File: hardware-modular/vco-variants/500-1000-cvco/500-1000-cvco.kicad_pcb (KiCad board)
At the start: 2 copper layers, 60 x 40 mm, 5 parts, among them J1 RF_IN

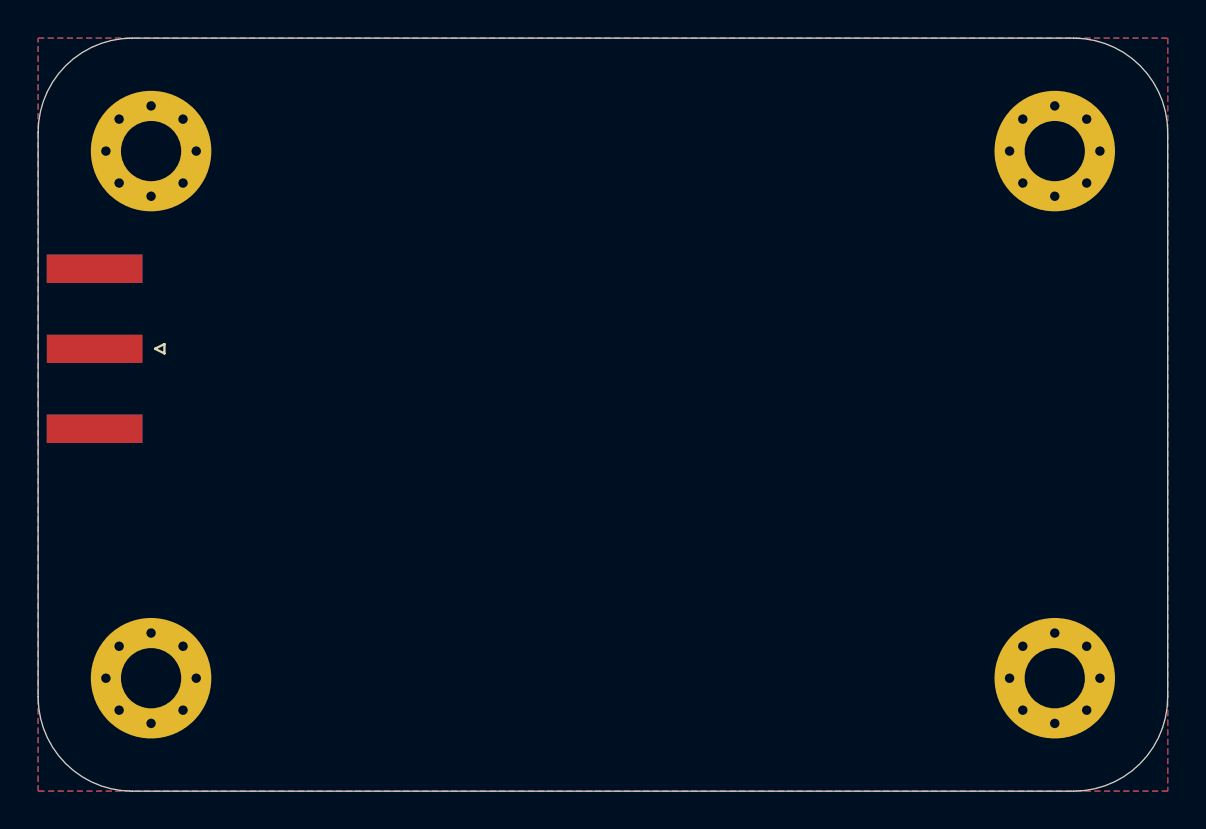
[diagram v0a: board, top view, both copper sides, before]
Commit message: CVCO 500-1000 MHz module - PCB.
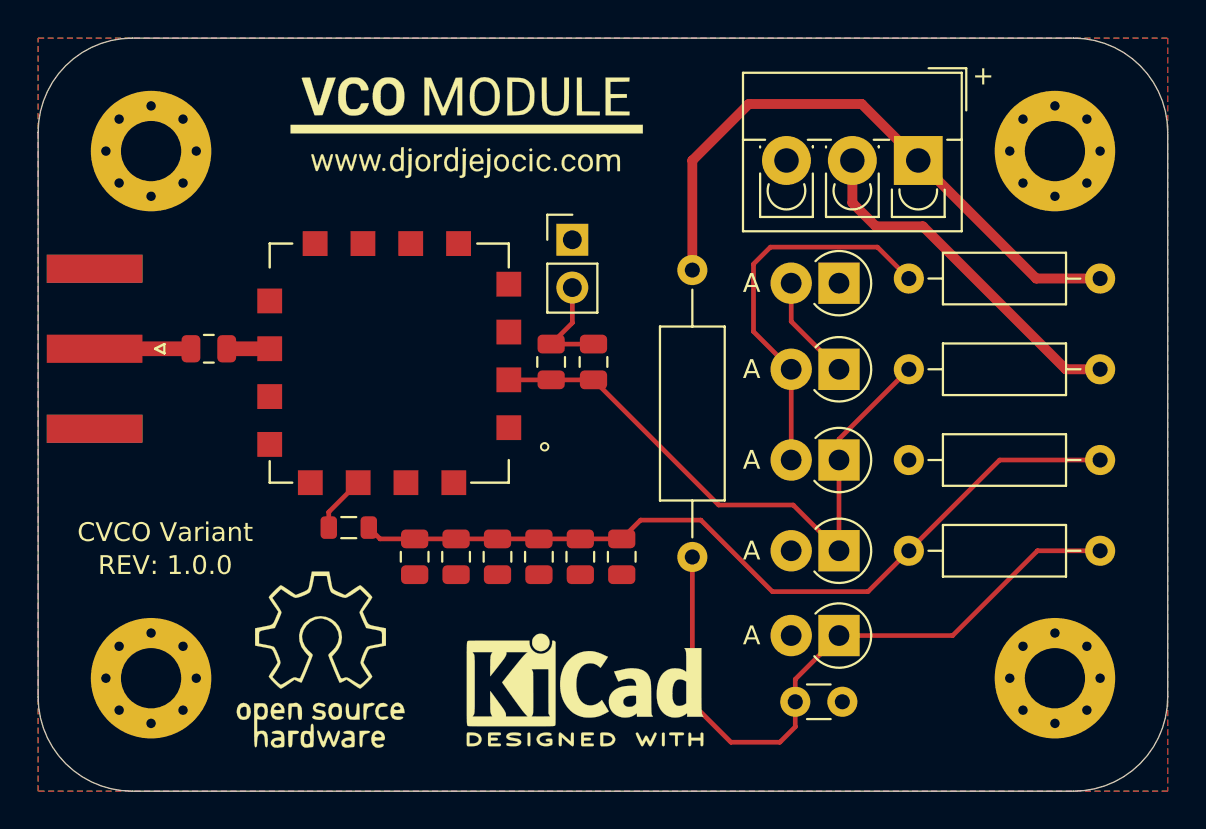
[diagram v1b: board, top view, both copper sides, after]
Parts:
- added C1: 1μF, Capacitor_THT:C_Disc_D3.0mm_W1.6mm_P2.50mm, F.Cu at (140.2, 85.2)
- added C10: 0.1μF, Capacitor_SMD:C_0805_2012Metric, F.Cu at (127.2, 67.2)
- added C2: 1μF, Capacitor_SMD:C_0805_2012Metric, F.Cu at (131.0, 77.5)
- added C3: 1μF, Capacitor_SMD:C_0805_2012Metric, F.Cu at (128.8, 77.5)
- added C4: 1.2nF, Capacitor_SMD:C_0805_2012Metric, F.Cu at (126.6, 77.5)
- added C5: 1.2nF, Capacitor_SMD:C_0805_2012Metric, F.Cu at (124.4, 77.5)
- added C6: 68pF, Capacitor_SMD:C_0805_2012Metric, F.Cu at (122.2, 77.5)
- added C7: 68pF, Capacitor_SMD:C_0805_2012Metric, F.Cu at (120.0, 77.5)
- added C8: 1.6nF, Capacitor_SMD:C_0805_2012Metric, F.Cu at (109.1, 66.5)
- added C9: 1μF, Capacitor_SMD:C_0805_2012Metric, F.Cu at (129.5, 67.2)
- added D1: ZPY 20, Diode_THT:D_DO-41_SOD81_P2.54mm_Vertical_AnodeUp, F.Cu at (142.5, 81.7)
- added D2: 1N4007, Diode_THT:D_DO-41_SOD81_P2.54mm_Vertical_AnodeUp, F.Cu at (142.5, 72.4)
- added D3: 1N4007, Diode_THT:D_DO-41_SOD81_P2.54mm_Vertical_AnodeUp, F.Cu at (142.5, 67.6)
- added D4: 1N4007, Diode_THT:D_DO-41_SOD81_P2.54mm_Vertical_AnodeUp, F.Cu at (142.5, 63.0)
- added D5: ZPY 18, Diode_THT:D_DO-41_SOD81_P2.54mm_Vertical_AnodeUp, F.Cu at (142.5, 77.2)
- added G***: LOGO, Icons:VCO_Module_Label, F.Cu at (122.8, 54.8)
- added G***: OSHW LOGO, Icons:OSHW, F.Cu at (115.0, 83.0)
- added J1: INPUT, TerminalBlock_4Ucon:TerminalBlock_4Ucon_1x03_P3.50mm_Vertical, F.Cu at (146.8, 56.5)
- added JP1: Jumper, Connector_PinHeader_2.54mm:PinHeader_1x02_P2.54mm_Vertical, F.Cu at (128.4, 60.7)
- added L1: 470μF, Inductor_SMD:L_0805_2012Metric, F.Cu at (116.5, 76.0)
- added R1: 670, Resistor_THT:R_Axial_DIN0309_L9.0mm_D3.2mm_P15.24mm_Horizontal, F.Cu at (134.8, 62.3)
- added R2: 1.2k, Resistor_THT:R_Axial_DIN0207_L6.3mm_D2.5mm_P10.16mm_Horizontal, F.Cu at (156.4, 77.2)
- added R3: 1.8k, Resistor_THT:R_Axial_DIN0207_L6.3mm_D2.5mm_P10.16mm_Horizontal, F.Cu at (156.4, 72.4)
- added R4: 3k, Resistor_THT:R_Axial_DIN0207_L6.3mm_D2.5mm_P10.16mm_Horizontal, F.Cu at (146.2, 62.8)
- added R5: 3k, Resistor_THT:R_Axial_DIN0207_L6.3mm_D2.5mm_P10.16mm_Horizontal, F.Cu at (146.2, 67.6)
- added REF**: KiCad-Logo2_5mm_SilkScreen, Symbol:KiCad-Logo2_5mm_SilkScreen, F.Cu at (129.0, 84.6)
- added Y1: 549-CV55CW500-1000, CVCO:CVCO55, F.Cu at (125.0, 73.6)
- J2: renamed from J1; value RF_IN -> RF_OUT
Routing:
- net Net-(C2-Pad1): track 0.00 -> 44.0 mm
- net Net-(C1-Pad1): track 0.00 -> 36.0 mm
- net +24V: track 0.00 -> 32.6 mm
- net Net-(C10-Pad1): track 0.00 -> 32.5 mm
- net Net-(D2-Pad2): track 0.00 -> 20.6 mm
- net TUNE: track 0.00 -> 19.1 mm
- net Net-(C10-Pad2): track 0.00 -> 5.72 mm
- net Net-(D3-Pad1): track 0.00 -> 5.63 mm
- net Net-(C8-Pad1): track 0.00 -> 5.12 mm
- net Net-(L1-Pad2): track 0.00 -> 3.03 mm
- net Net-(C8-Pad2): track 0.00 -> 2.28 mm
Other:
- board text added: "+"
- board text added: "CVCO Variant"
- board text added: "REV: 1.0.0"
